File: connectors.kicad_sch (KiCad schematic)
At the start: 32 parts, among them J1 USB_C_Receptacle, J2 Audio_Jack_Input, J3 Audio_Jack_Output, J4 UART_CONNECTOR, J5 JTAG 20-Pin, Q1 2N7002E, Q2 2N7002E, Q3 2N7002E, Q4 2N7002E

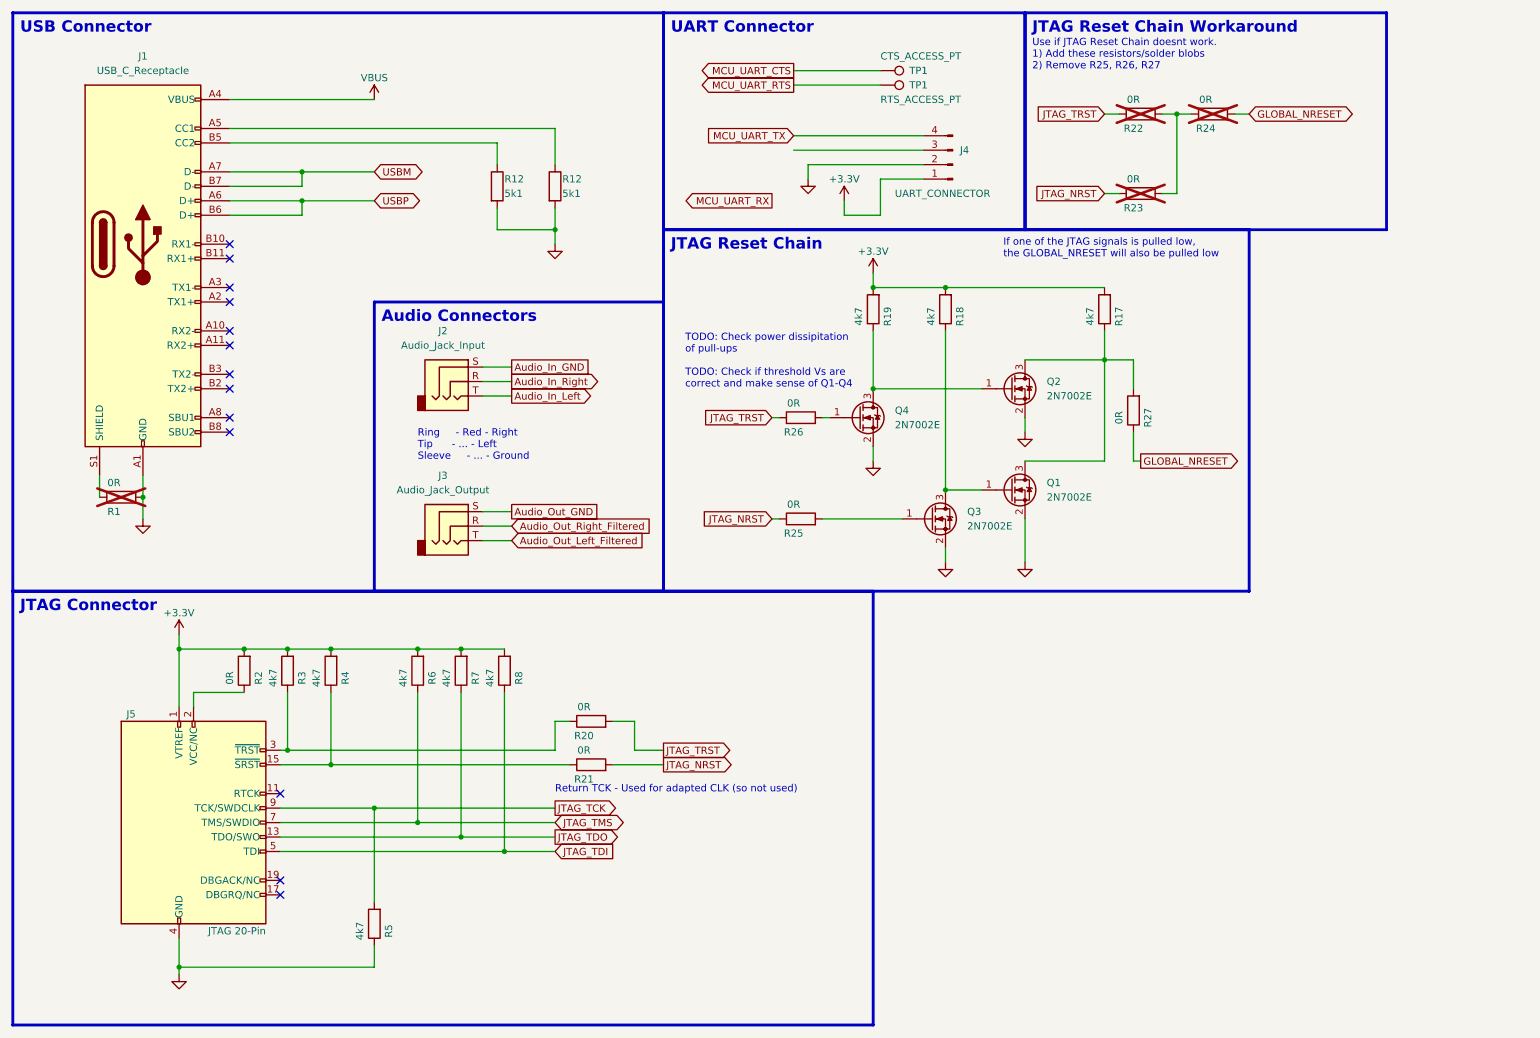
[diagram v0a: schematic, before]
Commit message: Added ESD, updated Footprints, BOM, etc.
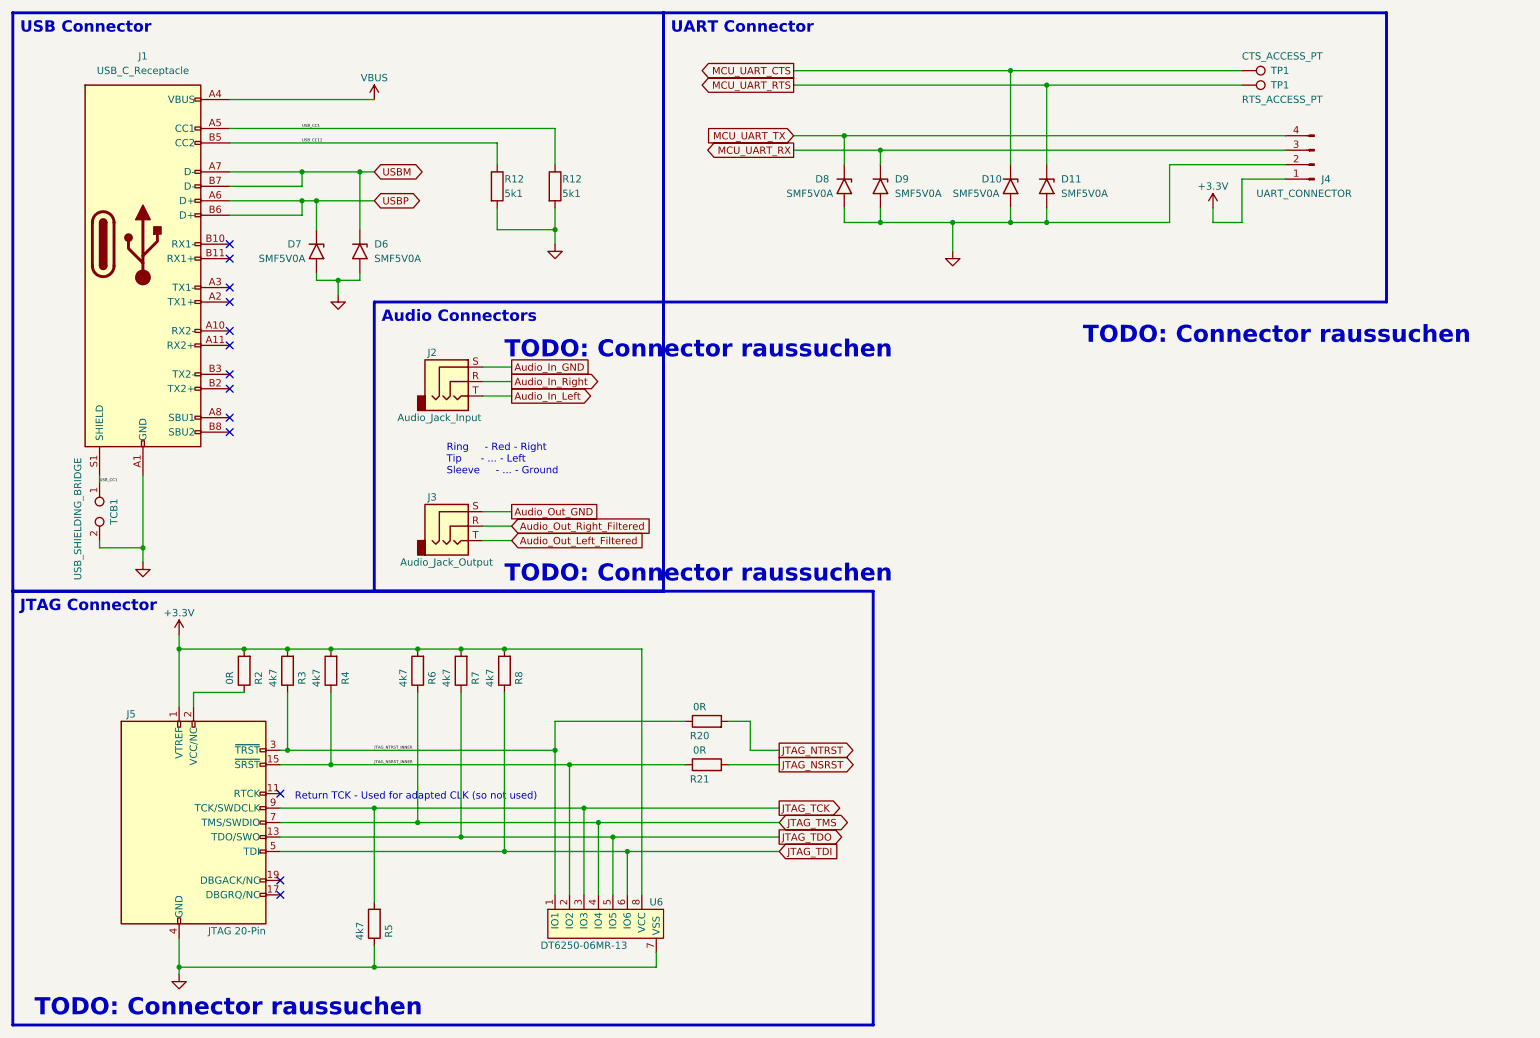
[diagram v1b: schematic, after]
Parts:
- removed Q1, Q2, Q3, Q4: 2N7002E, Package_TO_SOT_SMD:SOT-23, symbol Transistor_FET:2N7002E
- removed R1: 0R, Resistor_SMD:R_0805_2012Metric, symbol Device:R
- removed R17, R18, R19: 4k7, Resistor_SMD:R_0402_1005Metric, symbol Device:R
- removed R22, R23, R24, R25, R26, R27: 0R, Resistor_SMD:R_0402_1005Metric, symbol Device:R
- added D10, D11, D6, D7, D8, D9: SMF5V0A, Diode_SMD:D_SMF, symbol Diode:SMF5V0A
- added TCB1: USB_SHIELDING_BRIDGE, Jumper:SolderJumper-2_P1.3mm_Open_Pad1.0x1.5mm, symbol Connector:TestPoint_2Pole
- added U6: DT6250-06MR-13, Package_SO:MSOP-8_3x3mm_P0.65mm, symbol TimosSymbole:DT6250-06MR-13
- TP1: now left out of the parts list
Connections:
- net +3.3V: now also U6.8 (VCC)
- net GND: now also D10.2 (A2), D11.2 (A2), D6.2 (A2), D7.2 (A2), D8.2 (A2), D9.2 (A2), TCB1.2, U6.7 (VSS)
- net JTAG_TCK: now also U6.3 (IO3)
- net JTAG_TDI: now also U6.6 (IO6)
- net JTAG_TDO: now also U6.5 (IO5)
- net JTAG_TMS: now also U6.4 (IO4)
- net MCU_UART_CTS: now also D10.1 (A1)
- net MCU_UART_RTS: now also D11.1 (A1)
- net MCU_UART_RX: now also J4.3 (Pin_3), D9.1 (A1)
- net MCU_UART_TX: now also D8.1 (A1)
- net USBM: now also D6.1 (A1)
- net USBP: now also D7.1 (A1)
- net USB_CC1: now reaches J1.A5 (CC1), R12.1
- net USB_CC1: now also J1.S1 (SHIELD), TCB1.1
- net USB_CC12: now reaches J1.B5 (CC2), R12.1
- net JTAG_NSRST_INNER: now reaches J5.15 (~{SRST}), R21.1, R4.1
- net JTAG_NSRST_INNER: now also U6.2 (IO2)
- net JTAG_NTRST_INNER: now reaches J5.3 (~{TRST}), R20.1, R3.1
- net JTAG_NTRST_INNER: now also U6.1 (IO1)
- net JTAG_NRST renamed JTAG_NSRST
- net JTAG_TRST renamed JTAG_NTRST
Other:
- note added: "TODO: Connector raussuchen"
- note removed: "If one of the JTAG signals is pulled low, the GLOBAL_NRESET will also be pulled low"
- note removed: "JTAG Reset Chain"
- note removed: "JTAG Reset Chain Workaround"
- note removed: "TODO: Check power dissipitation of pull-ups TODO: Check if threshold Vs are correct and make sense of Q1-Q4"
- note removed: "Use if JTAG Reset Chain doesnt work. 1) Add these resistors/solder blobs 2) Remove R25, R26, R27"
- moved on the sheet: J4, R20, R21, TP1

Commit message: Schematic is done for now, starting layout
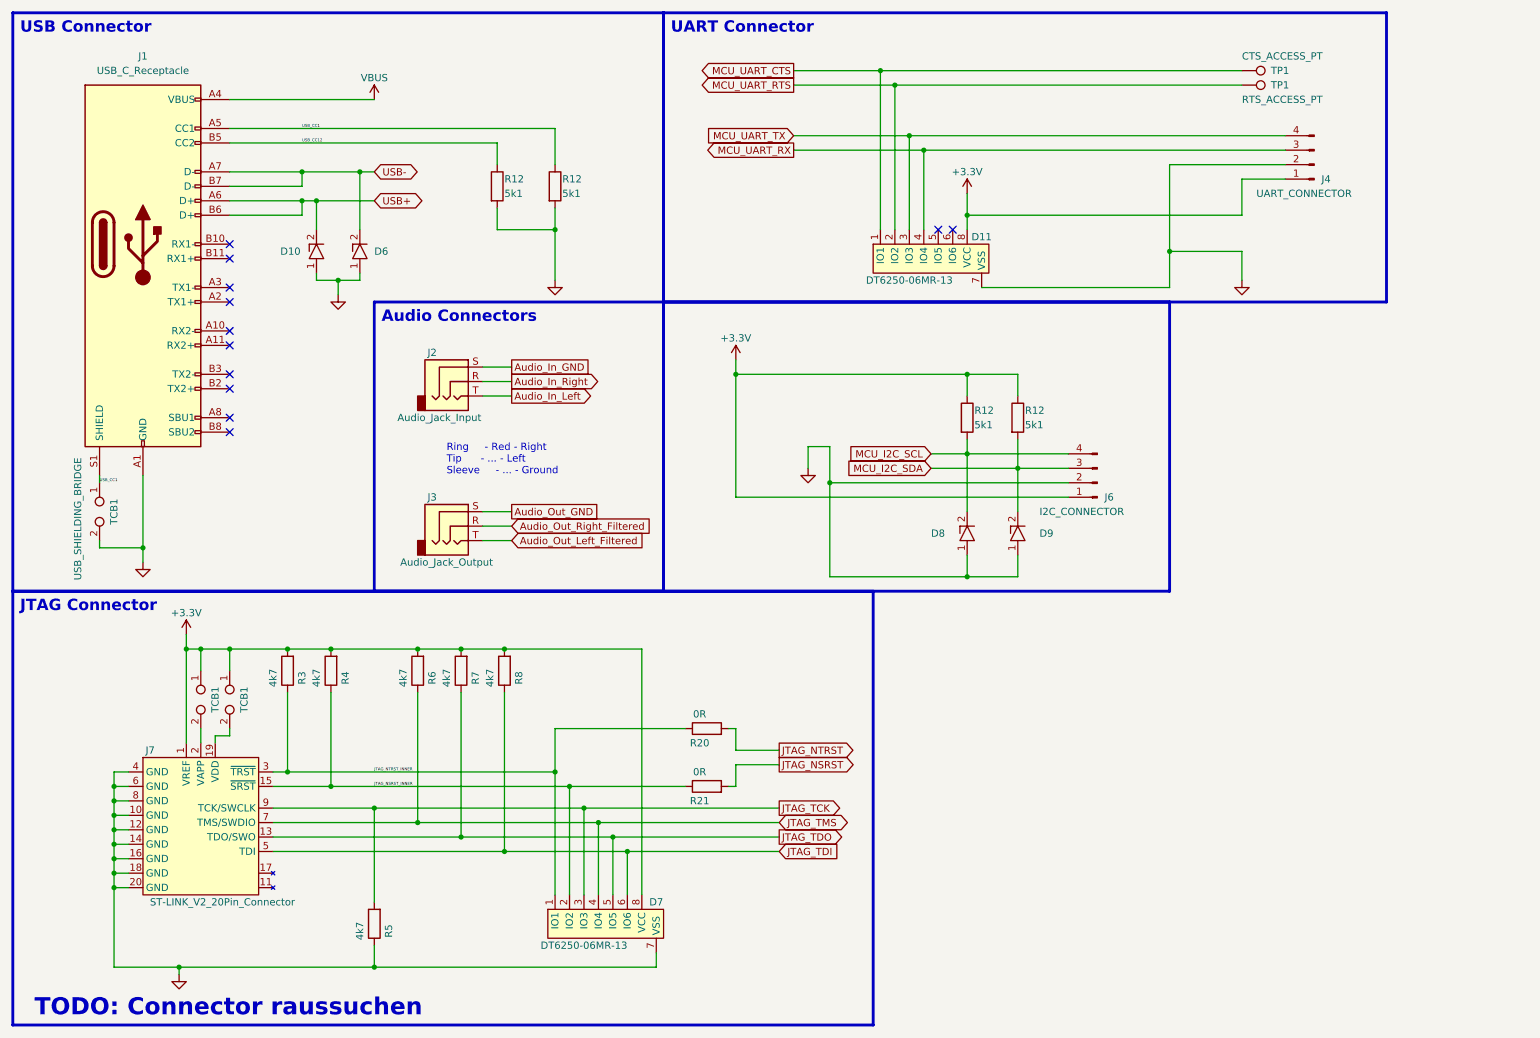
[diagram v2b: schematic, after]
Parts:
- removed D10, D11, D6, D7, D8, D9: SMF5V0A, Diode_SMD:D_SMF, symbol Diode:SMF5V0A
- removed J5: JTAG 20-Pin, Connector_PinHeader_2.54mm:PinHeader_2x10_P2.54mm_Vertical_SMD, symbol Connector:Conn_ARM_JTAG_SWD_20
- removed R2: 0R, Resistor_SMD:R_0805_2012Metric, symbol Device:R
- added D10, D6, D8, D9: TVSA04V05C006, TimosFootprints:TVSA04V05C006, symbol TimosSymbole:TVSA04V05C006
- added D11: DT6250-06MR-13, Package_SO:MSOP-8_3x3mm_P0.65mm, symbol TimosSymbole:DT6250-06MR-13
- added J6: I2C_CONNECTOR, Connector_PinHeader_2.54mm:PinHeader_1x04_P2.54mm_Vertical, symbol Connector:Conn_01x04_Pin
- added J7: ST-LINK_V2_20Pin_Connector, TimosFootprints:ST-LINK_V2_20Pin_Connector, symbol TimosSymbole:ST-LINK_V2_20Pin_Connector
- added R12 (x2): 5k1, Resistor_SMD:R_0603_1608Metric, symbol Device:R
- added TCB1 (x2): ~, Jumper:SolderJumper-2_P1.3mm_Open_Pad1.0x1.5mm, symbol Connector:TestPoint_2Pole
- D7: renamed from U6; Distributor Link (none) -> https://www.mouser.de/ProductDetail/Diodes-Incorporated/DT6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; Manufacturer (none) -> Diodes Incorporated; Manufacturer Number (none) -> DT6250-06MR-13
- J1: Distributor Link (none) -> https://www.mouser.de/ProductDetail/Molex/105450-0101?qs=sG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; Manufacturer (none) -> Molex; Manufacturer Number (none) -> 105450-0101
- J2, J3: Distributor Link (none) -> https://www.mouser.de/ProductDetail/CUI-Devices/SJ-3523-SMT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; Manufacturer (none) -> CUI Devices; Manufacturer Number (none) -> SJ-3523-SMT-TR
- J4: Distributor Link (none) -> https://www.mouser.de/ProductDetail/Harwin/M20-9770446?qs=u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; Manufacturer (none) -> Harwin; Manufacturer Number (none) -> M20-9770446
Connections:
- net +3.3V: now also D11.8 (VCC), J6.1 (Pin_1), J7.1 (VREF), R12.1, R12.1, TCB1.1, TCB1.1
- net GND: now also D10.1, D11.7 (VSS), D6.1, D8.1, D9.1, J6.2 (Pin_2), J7.10 (GND), J7.12 (GND), J7.14 (GND), J7.16 (GND), J7.18 (GND), J7.20 (GND), J7.4 (GND), J7.6 (GND), J7.8 (GND)
- net JTAG_NSRST_INNER: now also J7.15 (~{SRST})
- net JTAG_NTRST_INNER: now also J7.3 (~{TRST})
- net JTAG_TCK: now also J7.9 (TCK/SWCLK)
- net JTAG_TDI: now also J7.5 (TDI)
- net JTAG_TDO: now also J7.13 (TDO/SWO)
- net JTAG_TMS: now also J7.7 (TMS/SWDIO)
- net MCU_UART_CTS: now also D11.1 (IO1)
- net MCU_UART_RTS: now also D11.2 (IO2)
- net MCU_UART_RX: now also D11.4 (IO4)
- net MCU_UART_TX: now also D11.3 (IO3)
- net USBM renamed USB-
- net USB-: now also D6.2
- net USBP renamed USB+
- net USB+: now also D10.2
- new net: J7.2 (VAPP), TCB1.2
- new net: J7.19 (VDD), TCB1.2
- new net MCU_I2C_SCL: D8.2, J6.4 (Pin_4), R12.2
- new net MCU_I2C_SDA: D9.2, J6.3 (Pin_3), R12.2
- no-connect marks 13 -> 12
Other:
- note removed: "Return TCK - Used for adapted CLK (so not used)"
- moved on the sheet: R20, R21

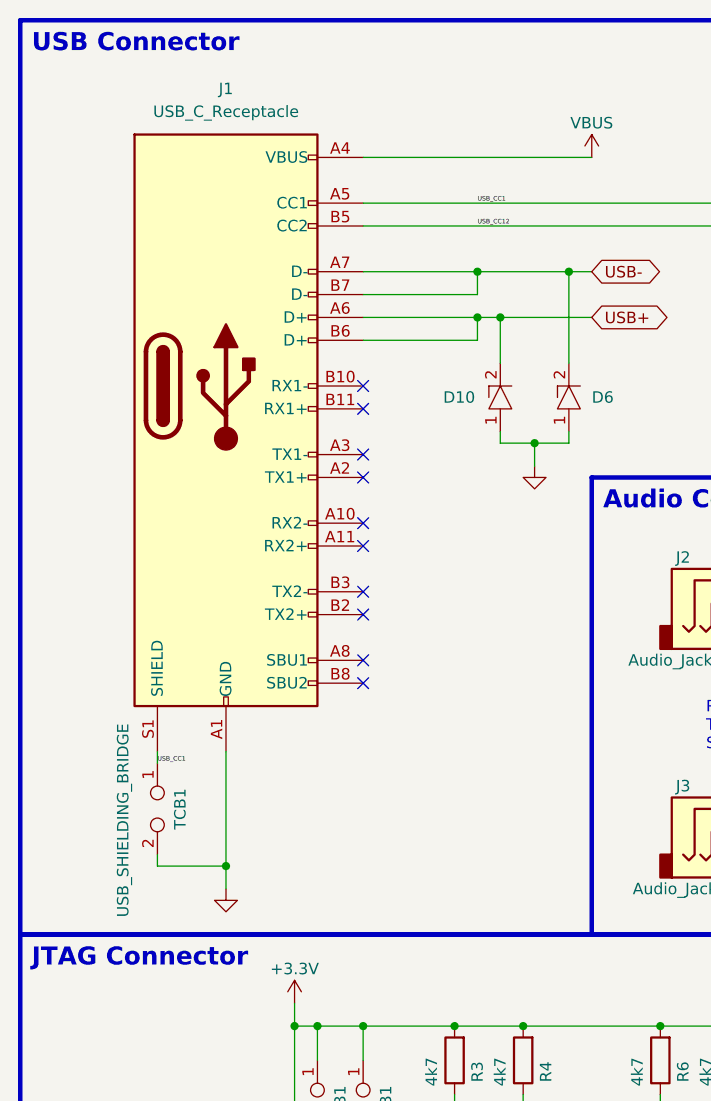
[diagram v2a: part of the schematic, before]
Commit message: Layout done, footprints mostly assigned, 3D models assigned if not annoying to get. Few TODOs left and they are marked on the PCB.
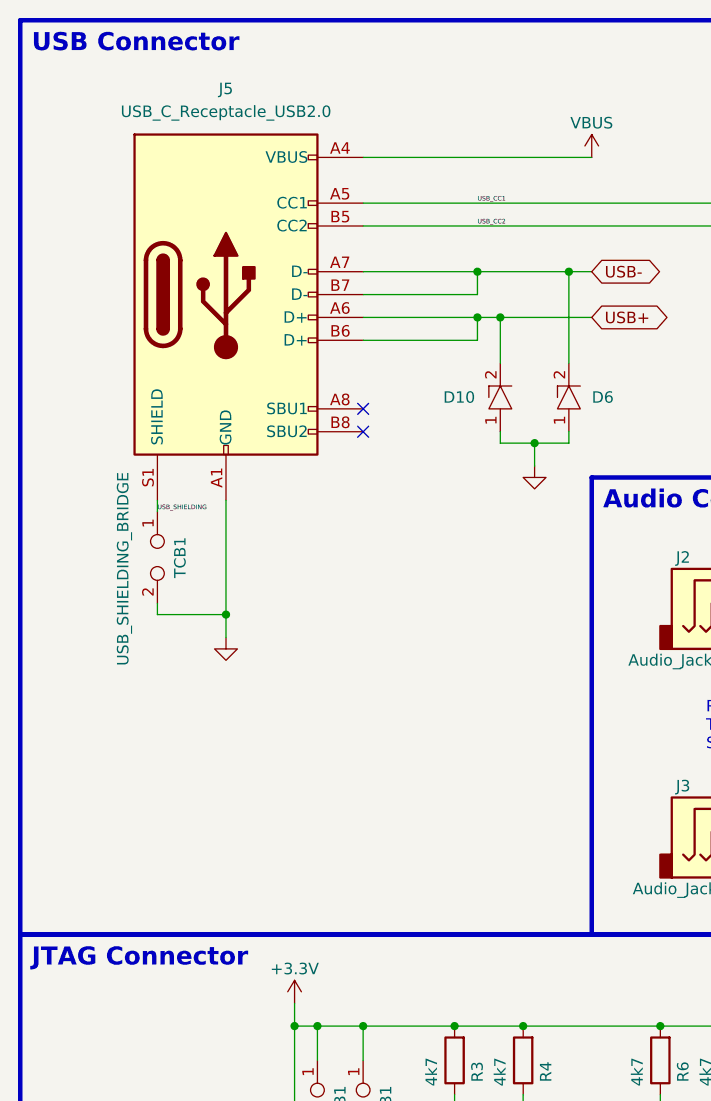
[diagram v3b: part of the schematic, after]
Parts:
- removed J1: USB_C_Receptacle, Connector_USB:USB_C_Receptacle_Molex_105450-0101, symbol Connector:USB_C_Receptacle
- added J5: USB_C_Receptacle_USB2.0, Connector_USB:USB_C_Receptacle_GCT_USB4105-xx-A_16P_TopMnt_Horizontal, symbol Connector:USB_C_Receptacle_USB2.0
- D11, D7: MFN DT6250-06MR-13 -> (none)
- J7: Distributor Link (none) -> https://www.mouser.de/ProductDetail/Molex/70246-2004?qs=sGA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; Manufacturer (none) -> Molex; Manufacturer Number (none) -> 70246-2004
- R12: footprint Resistor_SMD:R_0603_1608Metric -> Resistor_SMD:R_0402_1005Metric
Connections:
- net GND: now also J5.A1 (GND), J5.A12 (GND), J5.B1 (GND), J5.B12 (GND)
- net USB+: now also J5.A6 (D+), J5.B6 (D+)
- net USB-: now also J5.A7 (D-), J5.B7 (D-)
- net USB_CC1: now also J5.A5 (CC1); no longer TCB1.1
- net VBUS: now also J5.A4 (VBUS), J5.A9 (VBUS), J5.B4 (VBUS), J5.B9 (VBUS)
- net USB_CC12 renamed USB_CC2
- net USB_CC2: now also J5.B5 (CC2)
- new net USB_SHIELDING: J5.S1 (SHIELD), TCB1.1
- no-connect marks 12 -> 4
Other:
- moved on the sheet: TCB1
